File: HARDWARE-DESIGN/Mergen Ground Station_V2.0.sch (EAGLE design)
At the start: 68 parts, among them J1 USB_A_SMT_FEMALE_NS, J2 CON-SD-CARD_MICROSD-2908-05, J4 U.FL, U1 STM32F302C8T6, U13 L86, U15 AMS1117-5V, U16 AMS1117-3.3, X2 JST-XH-04-PIN-LONG-PAD, Y1 ABMM2-8.000MHZ-E2-T

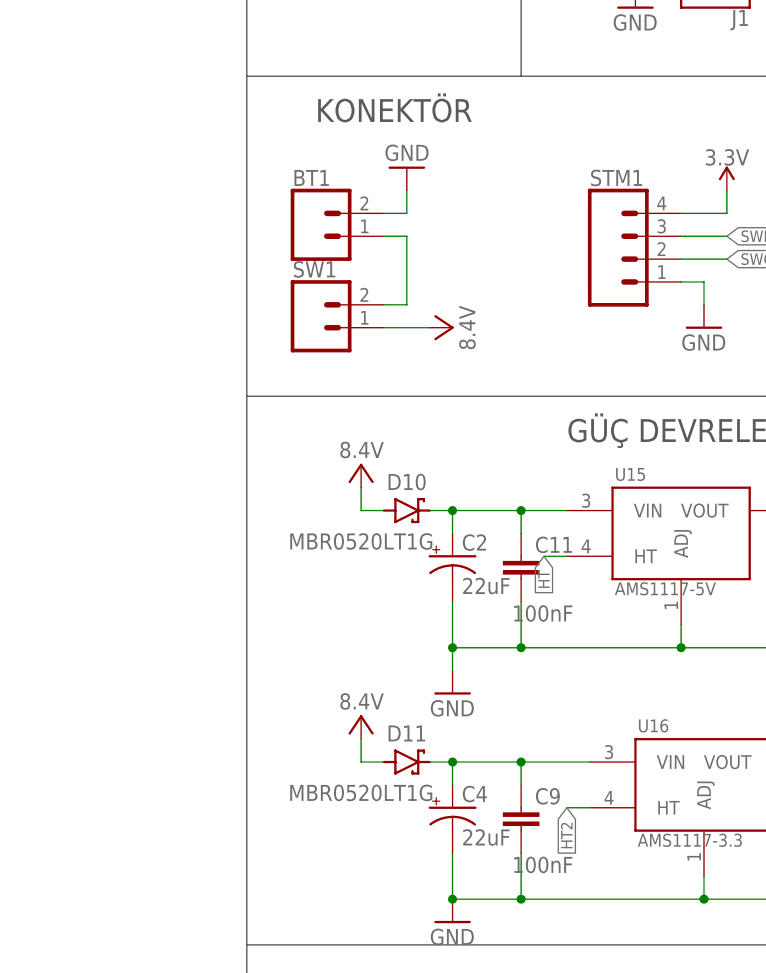
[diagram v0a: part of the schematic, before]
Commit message: Terminal Blocks were changed
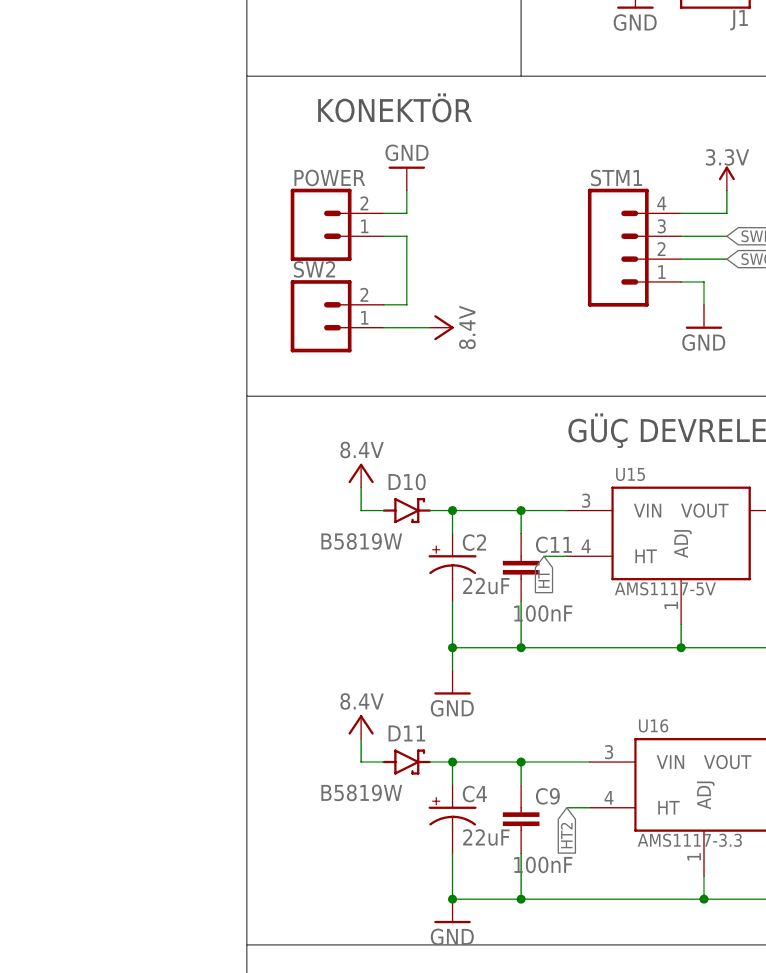
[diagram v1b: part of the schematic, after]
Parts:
- removed BT1, SW1: (no value), SparkFun-Connectors:CONN_02POLAR
- added POWER, SW2: (no value), SparkFun-Connectors:CONN_023.5MM-NO_SILK
- D10, D11: value MBR0520LT1G -> B5819W
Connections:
- net GND: now also POWER.2; no longer BT1.2
- net N$30: now also POWER.1, SW2.2; no longer BT1.1, SW1.2
- net VCC: now also SW2.1; no longer SW1.1
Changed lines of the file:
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@@
 <part name="U13" library="L86" deviceset="L86" device=""/>
 <part name="U14" library="E32-868T30S" deviceset="E32-868T30S" device=""/>
-<part name="BT1" library="SparkFun-Connectors" library_urn="urn:adsk.eagle:library:513" deviceset="CONN_02" device="POLAR" package3d_urn="urn:adsk.eagle:package:38040/1"/>
-<part name="D10" library="Diode" library_urn="urn:adsk.eagle:library:16378169" deviceset="SCHOTTKY_" device="DO-219" package3d_urn="urn:adsk.eagle:package:9427153/2" technology="MBR0520LT1G" value="MBR0520LT1G"/>
+<part name="D10" library="Diode" library_urn="urn:adsk.eagle:library:16378169" deviceset="SCHOTTKY_" device="DO-219" package3d_urn="urn:adsk.eagle:package:9427153/2" technology="MBR0520LT1G" value="B5819W"/>
 <part name="P+2" library="supply1" library_urn="urn:adsk.eagle:library:371" deviceset="VCC" device="" value="8.4V"/>
 <part name="F2" library="SparkFun-Fuses" library_urn="urn:adsk.eagle:library:517" deviceset="PPTC" device="_HALF-AMP" package3d_urn="urn:adsk.eagle:package:38575/1" value="1A"/>
-<part name="D11" library="Diode" library_urn="urn:adsk.eagle:library:16378169" deviceset="SCHOTTKY_" device="DO-219" package3d_urn="urn:adsk.eagle:package:9427153/2" technology="MBR0520LT1G" value="MBR0520LT1G"/>
+<part name="D11" library="Diode" library_urn="urn:adsk.eagle:library:16378169" deviceset="SCHOTTKY_" device="DO-219" package3d_urn="urn:adsk.eagle:package:9427153/2" technology="MBR0520LT1G" value="B5819W"/>
 <part name="P+4" library="supply1" library_urn="urn:adsk.eagle:library:371" deviceset="VCC" device="" value="8.4V"/>
 <part name="F4" library="SparkFun-Fuses" library_urn="urn:adsk.eagle:library:517" deviceset="PPTC" device="_HALF-AMP" package3d_urn="urn:adsk.eagle:package:38575/1" value="0.75A"/>
@@
 <part name="SUPPLY21" library="SparkFun-PowerSymbols" library_urn="urn:adsk.eagle:library:530" deviceset="3.3V" device=""/>
 <part name="SUPPLY22" library="SparkFun-PowerSymbols" library_urn="urn:adsk.eagle:library:530" deviceset="5V" device=""/>
-<part name="SW1" library="SparkFun-Connectors" library_urn="urn:adsk.eagle:library:513" deviceset="CONN_02" device="POLAR" package3d_urn="urn:adsk.eagle:package:38040/1"/>
 <part name="GND51" library="supply1" library_urn="urn:adsk.eagle:library:371" deviceset="GND" device=""/>
 <part name="GND52" library="supply1" library_urn="urn:adsk.eagle:library:371" deviceset="GND" device=""/>
@@
 <part name="SUPPLY7" library="SparkFun-PowerSymbols" library_urn="urn:adsk.eagle:library:530" deviceset="5V" device=""/>
 <part name="GND9" library="supply1" library_urn="urn:adsk.eagle:library:371" deviceset="GND" device=""/>
+<part name="POWER" library="SparkFun-Connectors" library_urn="urn:adsk.eagle:library:513" deviceset="CONN_02" device="3.5MM-NO_SILK" package3d_urn="urn:adsk.eagle:package:38055/1"/>
+<part name="SW2" library="SparkFun-Connectors" library_urn="urn:adsk.eagle:library:513" deviceset="CONN_02" device="3.5MM-NO_SILK" package3d_urn="urn:adsk.eagle:package:38055/1"/>
 </parts>
 <sheets>
@@
 </instance>
 <instance part="U14" gate="G$1" x="48.26" y="22.86" smashed="yes"/>
-<instance part="BT1" gate="G$1" x="-76.2" y="63.5" smashed="yes">
-<attribute name="VALUE" x="-78.74" y="58.674" size="1.778" layer="96" font="vector"/>
-<attribute name="NAME" x="-78.74" y="69.088" size="1.778" layer="95" font="vector"/>
-</instance>
 <instance part="D10" gate="G$1" x="-66.04" y="33.02" smashed="yes">
 <attribute name="NAME" x="-66.04" y="36.195" size="1.778" layer="95" align="center"/>
@@
 <attribute name="VALUE" x="22.86" y="35.814" size="1.778" layer="96" align="bottom-center"/>
 </instance>
-<instance part="SW1" gate="G$1" x="-76.2" y="53.34" smashed="yes">
-<attribute name="VALUE" x="-78.74" y="48.514" size="1.778" layer="96" font="vector"/>
-<attribute name="NAME" x="-78.74" y="58.928" size="1.778" layer="95" font="vector"/>
-</instance>
 <instance part="GND51" gate="1" x="187.96" y="-88.9" smashed="yes">
 <attribute name="VALUE" x="182.88" y="-91.44" size="1.778" layer="96"/>
@@
 <instance part="GND9" gate="1" x="-66.04" y="93.98" smashed="yes">
 <attribute name="VALUE" x="-68.58" y="91.44" size="1.778" layer="96"/>
+</instance>
+<instance part="POWER" gate="G$1" x="-76.2" y="63.5" smashed="yes">
+<attribute name="VALUE" x="-78.74" y="58.674" size="1.778" layer="96" font="vector"/>
+<attribute name="NAME" x="-78.74" y="69.088" size="1.778" layer="95" font="vector"/>
+</instance>
+<instance part="SW2" gate="G$1" x="-76.2" y="53.34" smashed="yes">
+<attribute name="VALUE" x="-78.74" y="48.514" size="1.778" layer="96" font="vector"/>
+<attribute name="NAME" x="-78.74" y="58.928" size="1.778" layer="95" font="vector"/>
 </instance>
 </instances>
@@
 </segment>
 <segment>
-<pinref part="SW1" gate="G$1" pin="1"/>
 <wire x1="-68.58" y1="53.34" x2="-63.5" y2="53.34" width="0.1524" layer="91"/>
 <pinref part="P+5" gate="VCC" pin="VCC"/>
+<pinref part="SW2" gate="G$1" pin="1"/>
 </segment>
 </net>
@@
 </segment>
 <segment>
-<pinref part="BT1" gate="G$1" pin="2"/>
 <wire x1="-68.58" y1="66.04" x2="-66.04" y2="66.04" width="0.1524" layer="91"/>
 <pinref part="GND44" gate="1" pin="GND"/>
 <wire x1="-66.04" y1="66.04" x2="-66.04" y2="68.58" width="0.1524" layer="91"/>
+<pinref part="POWER" gate="G$1" pin="2"/>
 </segment>
 <segment>
@@
 <net name="N$30" class="0">
 <segment>
-<pinref part="BT1" gate="G$1" pin="1"/>
 <wire x1="-68.58" y1="63.5" x2="-66.04" y2="63.5" width="0.1524" layer="91"/>
-<pinref part="SW1" gate="G$1" pin="2"/>
 <wire x1="-68.58" y1="55.88" x2="-66.04" y2="55.88" width="0.1524" layer="91"/>
 <wire x1="-66.04" y1="55.88" x2="-66.04" y2="63.5" width="0.1524" layer="91"/>
-</segment>
-</net>
+<pinref part="POWER" gate="G$1" pin="1"/>
+<pinref part="SW2" gate="G$1" pin="2"/>
+</segment>
+</net>

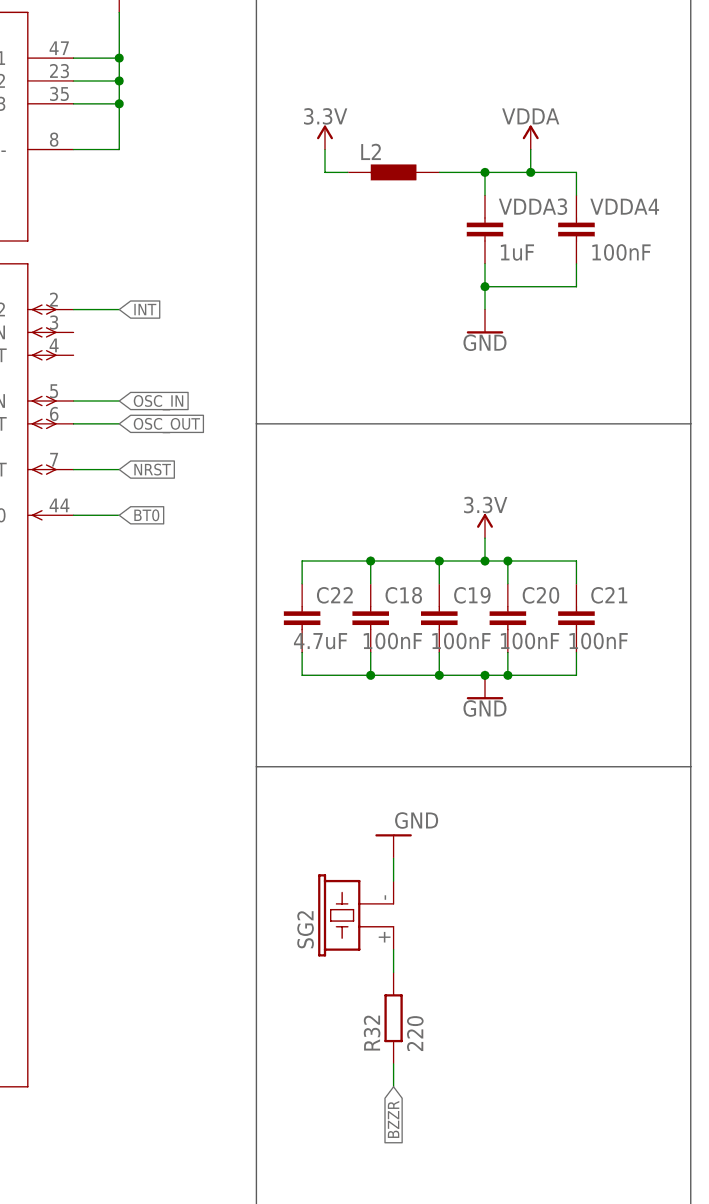
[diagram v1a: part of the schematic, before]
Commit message: packages was modified according to stock situation
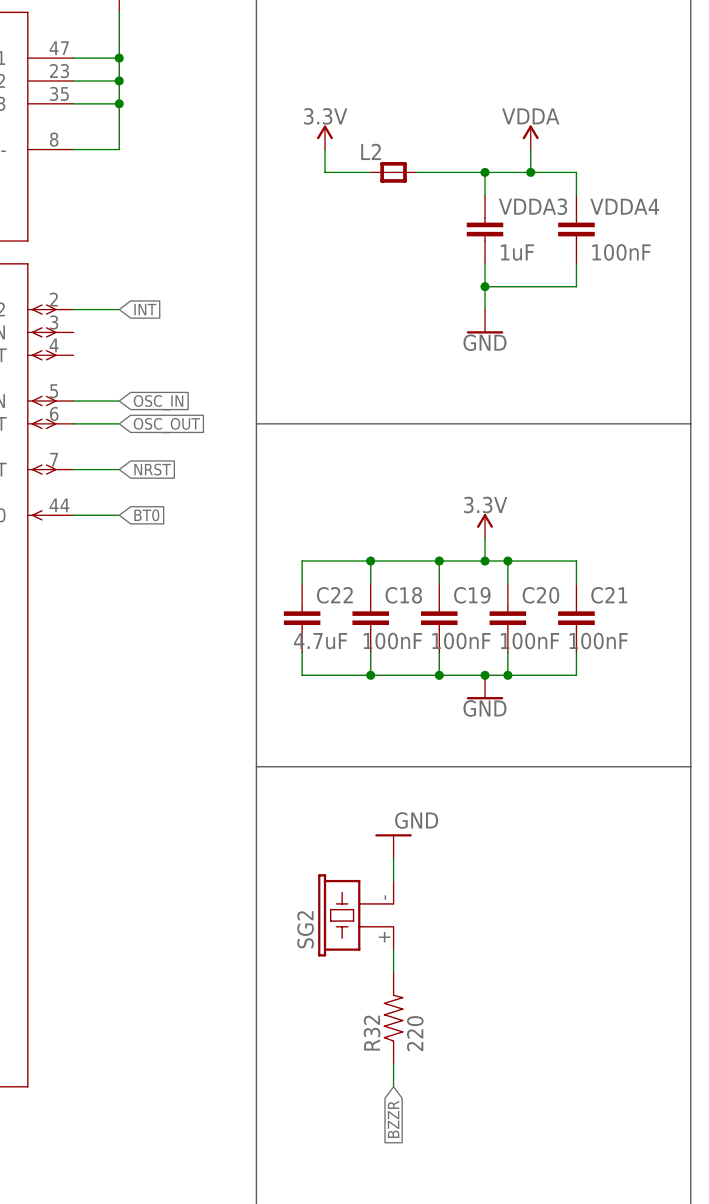
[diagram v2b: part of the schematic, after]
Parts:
- C42: device rcl:CPOL-USR/2012-12W -> SparkFun-Capacitors:10UF-POLAR-EIA3216-16V-10%(TANT)
- L2: value BLM15HB221SN1 -> (none); device inductors:BLM15HB221SN1 -> 52101-101-REV-A_v16:RC-MASTER-SMD_FB_0805MP
- R32: device rcl:R-EU_R0402 -> SparkFun-Resistors:0OHM-0603-1/10W-5%
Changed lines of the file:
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@@
 <part name="GND48" library="supply1" library_urn="urn:adsk.eagle:library:371" deviceset="GND" device=""/>
 <part name="SG2" library="buzzer" library_urn="urn:adsk.eagle:library:113" deviceset="F/CM12P" device="" package3d_urn="urn:adsk.eagle:package:5265/1"/>
-<part name="R32" library="rcl" library_urn="urn:adsk.eagle:library:334" deviceset="R-EU_" device="R0402" package3d_urn="urn:adsk.eagle:package:23547/3" value="220"/>
+<part name="R32" library="SparkFun-Resistors" library_urn="urn:adsk.eagle:library:532" deviceset="0OHM" device="-0603-1/10W-5%" package3d_urn="urn:adsk.eagle:package:39650/1" value="220"/>
 <part name="GND49" library="supply1" library_urn="urn:adsk.eagle:library:371" deviceset="GND" device=""/>
 <part name="SUPPLY19" library="SparkFun-PowerSymbols" library_urn="urn:adsk.eagle:library:530" deviceset="3.3V" device=""/>
@@
 <part name="D15" library="SparkFun-LED" library_urn="urn:adsk.eagle:library:27167846" deviceset="LED" device="0603" package3d_urn="urn:adsk.eagle:package:27167834/2"/>
 <part name="D16" library="SparkFun-LED" library_urn="urn:adsk.eagle:library:27167846" deviceset="LED" device="0603" package3d_urn="urn:adsk.eagle:package:27167834/2"/>
-<part name="C42" library="rcl" library_urn="urn:adsk.eagle:library:334" deviceset="CPOL-US" device="R/2012-12W" package3d_urn="urn:adsk.eagle:package:23419/2" value="10uF"/>
+<part name="C42" library="SparkFun-Capacitors" library_urn="urn:adsk.eagle:library:27162641" deviceset="10UF-POLAR" device="-EIA3216-16V-10%(TANT)" package3d_urn="urn:adsk.eagle:package:37418/1" value="10uF"/>
 <part name="J4" library="SparkFun-Connectors" deviceset="U.FL2PIN" device="" value="U.FL"/>
 <part name="GND58" library="SparkFun-PowerSymbols" deviceset="GND" device=""/>
@@
 <part name="VDDA4" library="SparkFun-Capacitors" library_urn="urn:adsk.eagle:library:510" deviceset="0.1UF" device="-0603-25V-(+80/-20%)" package3d_urn="urn:adsk.eagle:package:37414/1" value="100nF"/>
 <part name="GND72" library="SparkFun-PowerSymbols" library_urn="urn:adsk.eagle:library:530" deviceset="GND" device=""/>
-<part name="L2" library="inductors" library_urn="urn:adsk.eagle:library:243" deviceset="BLM15H" device="" package3d_urn="urn:adsk.eagle:package:15132/1" technology="B221SN1"/>
+<part name="L2" library="52101-101-REV-A_v16" library_urn="urn:adsk.eagle:library:21899384" deviceset="RC-MASTER-SMD_FB_" device="0805MP" package3d_urn="urn:adsk.eagle:package:15662270/2"/>
 <part name="SUPPLY37" library="SparkFun-PowerSymbols" library_urn="urn:adsk.eagle:library:530" deviceset="3.3V" device=""/>
 <part name="U$5" library="SparkFun-PowerSymbols" library_urn="urn:adsk.eagle:library:530" deviceset="VDDA" device=""/>
@@
 <wire x1="185.42" y1="60.96" x2="185.42" y2="58.42" width="0.1524" layer="91"/>
 <pinref part="L2" gate="G$1" pin="1"/>
-<wire x1="185.42" y1="58.42" x2="187.96" y2="58.42" width="0.1524" layer="91"/>
+<wire x1="185.42" y1="58.42" x2="190.5" y2="58.42" width="0.1524" layer="91"/>
 </segment>
 <segment>
@@
 <pinref part="L2" gate="G$1" pin="2"/>
 <pinref part="VDDA4" gate="G$1" pin="1"/>
-<wire x1="198.12" y1="58.42" x2="203.2" y2="58.42" width="0.1524" layer="91"/>
+<wire x1="195.58" y1="58.42" x2="203.2" y2="58.42" width="0.1524" layer="91"/>
 <wire x1="203.2" y1="58.42" x2="208.28" y2="58.42" width="0.1524" layer="91"/>
 <wire x1="208.28" y1="58.42" x2="213.36" y2="58.42" width="0.1524" layer="91"/>
